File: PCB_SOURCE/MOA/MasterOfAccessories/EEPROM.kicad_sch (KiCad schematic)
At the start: 2 parts, among them U801 24LC256

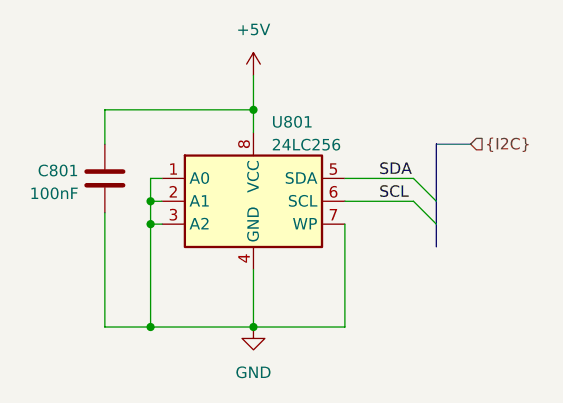
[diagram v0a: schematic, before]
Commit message: fixed bug in ahob program among others
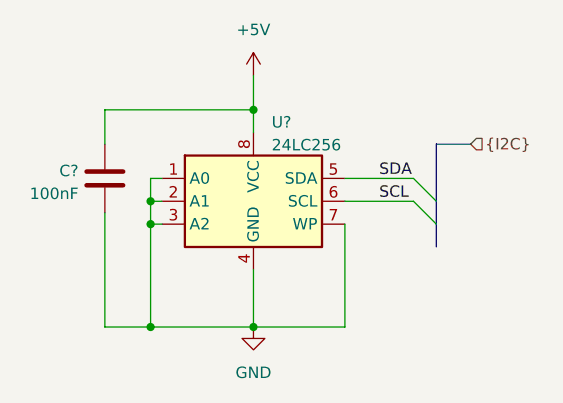
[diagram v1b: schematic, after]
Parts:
- renumbered C801 to C?, U801 to U?
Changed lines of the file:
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@@
 	(label "SDA"
 		(at 116.84 68.58 0)
-		(fields_autoplaced yes)
 		(effects
 			(font
@@
 	(label "SCL"
 		(at 116.84 71.12 0)
-		(fields_autoplaced yes)
 		(effects
 			(font
@@
 		(shape input)
 		(at 127 64.77 0)
-		(fields_autoplaced yes)
 		(effects
 			(font
@@
 		(dnp no)
 		(fields_autoplaced yes)
-		(property "Reference" "#PWR0801"
+		(property "Reference" "#PWR?"
 			(at 102.87 60.96 0)
 			(effects
@@
 			(project "EEPROM"
 				(path "/7726f3b0-6d28-4a62-ae77-022bfbf3ad3f"
-					(reference "#PWR0801")
+					(reference "#PWR?")
 					(unit 1)
 				)
@@
 			(project "MasterOfAccessories"
 				(path "/d28c018f-83ab-41ca-9c80-395a46ff97ad/f3268e40-3e30-4729-953d-ad706ea621b4"
-					(reference "#PWR0801")
+					(reference "#PWR0901")
 					(unit 1)
 				)
@@
 			(project "general_schematics"
 				(path "/e777d9ec-d073-4229-a9e6-2cf85636e407/061d5b60-6a9d-4005-baf0-f56c3f730e99"
-					(reference "#PWR0154")
+					(reference "#PWR?")
 					(unit 1)
 				)
@@
 		(dnp no)
 		(fields_autoplaced yes)
-		(property "Reference" "U801"
+		(property "Reference" "U?"
 			(at 104.8894 62.3402 0)
 			(effects
@@
 			(project "EEPROM"
 				(path "/7726f3b0-6d28-4a62-ae77-022bfbf3ad3f"
-					(reference "U801")
+					(reference "U?")
 					(unit 1)
 				)
@@
 			(project "MasterOfAccessories"
 				(path "/d28c018f-83ab-41ca-9c80-395a46ff97ad/f3268e40-3e30-4729-953d-ad706ea621b4"
-					(reference "U801")
+					(reference "U901")
 					(unit 1)
 				)
@@
 			(project "general_schematics"
 				(path "/e777d9ec-d073-4229-a9e6-2cf85636e407/061d5b60-6a9d-4005-baf0-f56c3f730e99"
-					(reference "U1901")
+					(reference "U?")
 					(unit 1)
 				)
@@
 		(dnp no)
 		(fields_autoplaced yes)
-		(property "Reference" "#PWR0802"
+		(property "Reference" "#PWR?"
 			(at 102.87 91.44 0)
 			(effects
@@
 			(project "EEPROM"
 				(path "/7726f3b0-6d28-4a62-ae77-022bfbf3ad3f"
-					(reference "#PWR0802")
+					(reference "#PWR?")
 					(unit 1)
 				)
@@
 			(project "MasterOfAccessories"
 				(path "/d28c018f-83ab-41ca-9c80-395a46ff97ad/f3268e40-3e30-4729-953d-ad706ea621b4"
-					(reference "#PWR0802")
+					(reference "#PWR0902")
 					(unit 1)
 				)
@@
 		(dnp no)
 		(fields_autoplaced yes)
-		(property "Reference" "C801"
+		(property "Reference" "C?"
 			(at 83.439 67.7453 0)
 			(effects
@@
 			(project "EEPROM"
 				(path "/7726f3b0-6d28-4a62-ae77-022bfbf3ad3f"
-					(reference "C801")
+					(reference "C?")
 					(unit 1)
 				)
@@
 			(project "MasterOfAccessories"
 				(path "/d28c018f-83ab-41ca-9c80-395a46ff97ad/f3268e40-3e30-4729-953d-ad706ea621b4"
-					(reference "C801")
+					(reference "C901")
 					(unit 1)
 				)
@@
 			(project "general_schematics"
 				(path "/e777d9ec-d073-4229-a9e6-2cf85636e407/061d5b60-6a9d-4005-baf0-f56c3f730e99"
-					(reference "C1901")
-					(unit 1)
-				)
+					(reference "C?")
+					(unit 1)
+				)
